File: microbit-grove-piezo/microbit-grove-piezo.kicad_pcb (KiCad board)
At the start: 2 copper layers, 59 x 15.4 mm, 6 parts, among them J1 microbit_smd_socket, J2 0 13 + 1, J3 1 14 + -, J4 2 15 + -, J5 19 20 I2C + -

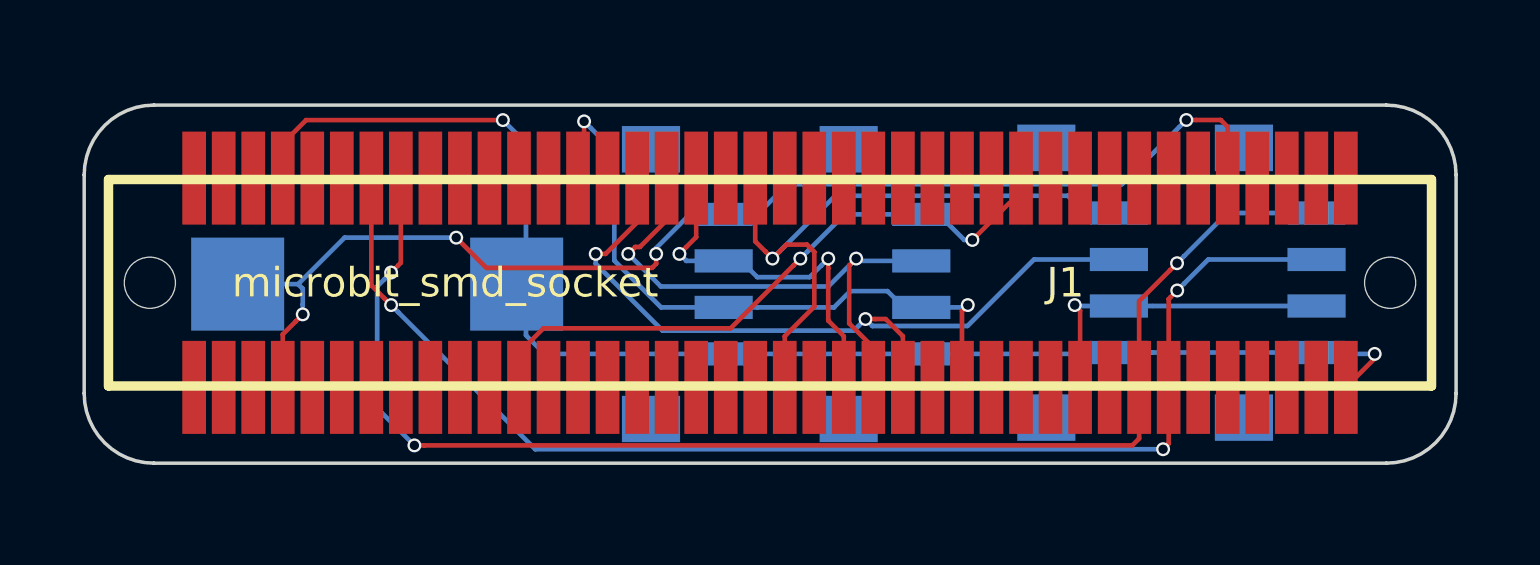
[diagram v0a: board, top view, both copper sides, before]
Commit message: Add logos to grove/piezo board
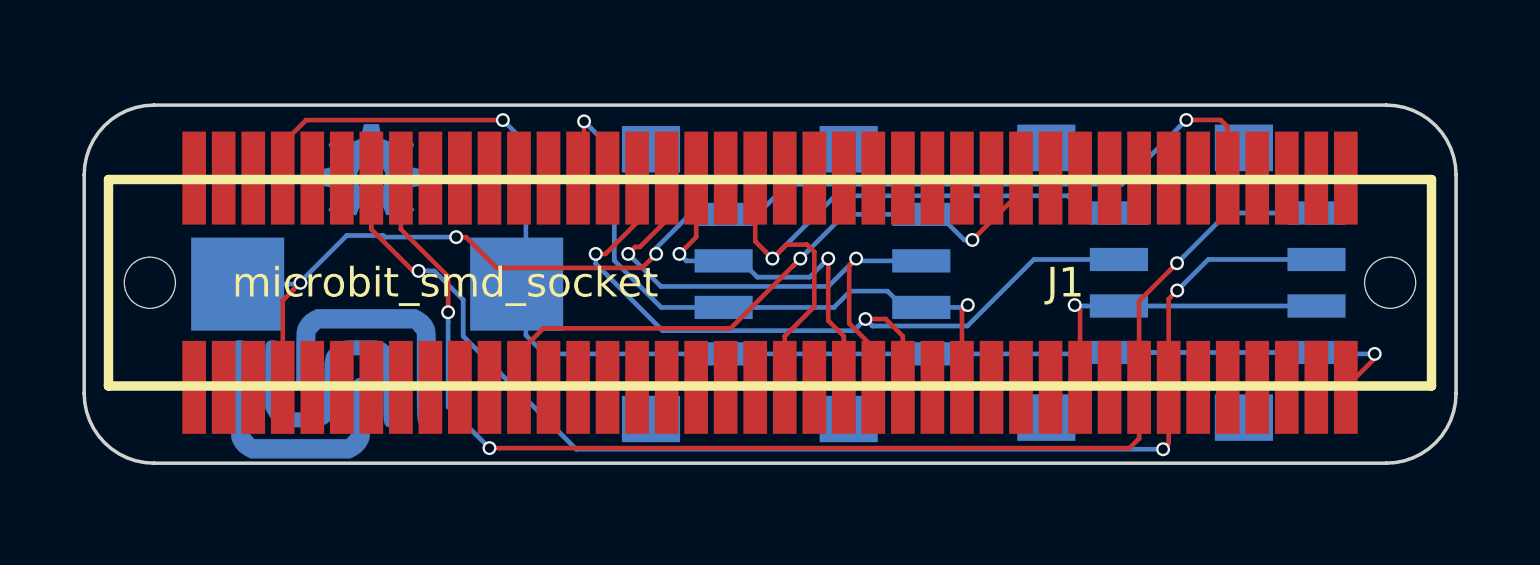
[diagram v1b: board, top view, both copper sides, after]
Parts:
- added Z1: ncss, logos:ncss, B.Cu at (131.6, 95.5)
- added Z2: oshw, logos:OSHW-Logo2_7.3x6mm_Copper, B.Cu at (133.3, 87.4)
- J2: value 0 13 + 1 -> GROVE-CONNECTOR-SMD_4+2P-2.0_
- J3: value 1 14 + - -> GROVE-CONNECTOR-SMD_4+2P-2.0_
- J4: value 2 15 + - -> GROVE-CONNECTOR-SMD_4+2P-2.0_
- J5: value 19 20 I2C + - -> GROVE-CONNECTOR-SMD_4+2P-2.0_
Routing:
- net MB_19: track 59.0 -> 56.4 mm

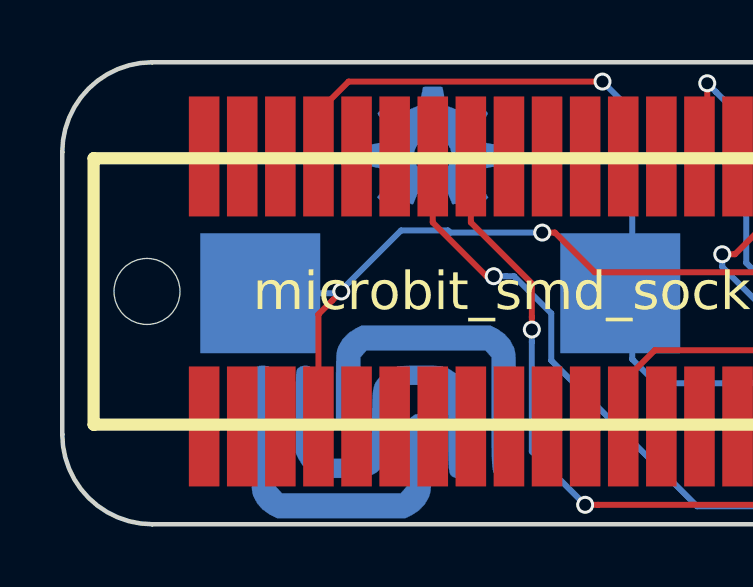
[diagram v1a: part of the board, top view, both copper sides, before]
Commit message: Make small logos for the grove board.
Test run gerbers.
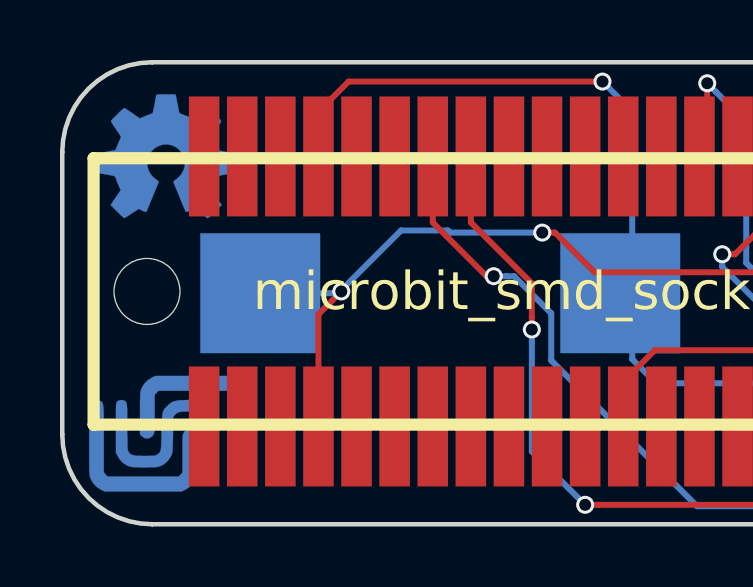
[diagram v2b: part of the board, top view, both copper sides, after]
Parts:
- Z1: footprint logos:ncss -> logos:ncss_small
- Z2: footprint logos:OSHW-Logo2_7.3x6mm_Copper -> logos:OSHW-Logo2_7.3x6mm_Copper_NoText
- moved Z2 8.89 mm to (124.5, 87.6)
- moved Z1 7.13 mm to (124.5, 96.0)
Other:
- board text added: "0 13 + -"
- board text added: "1 14 + -"
- board text added: "19 20 I2C + -"
- board text added: "2 15 + -"
- board text added: "github.com/jimmo/microbit-boards"

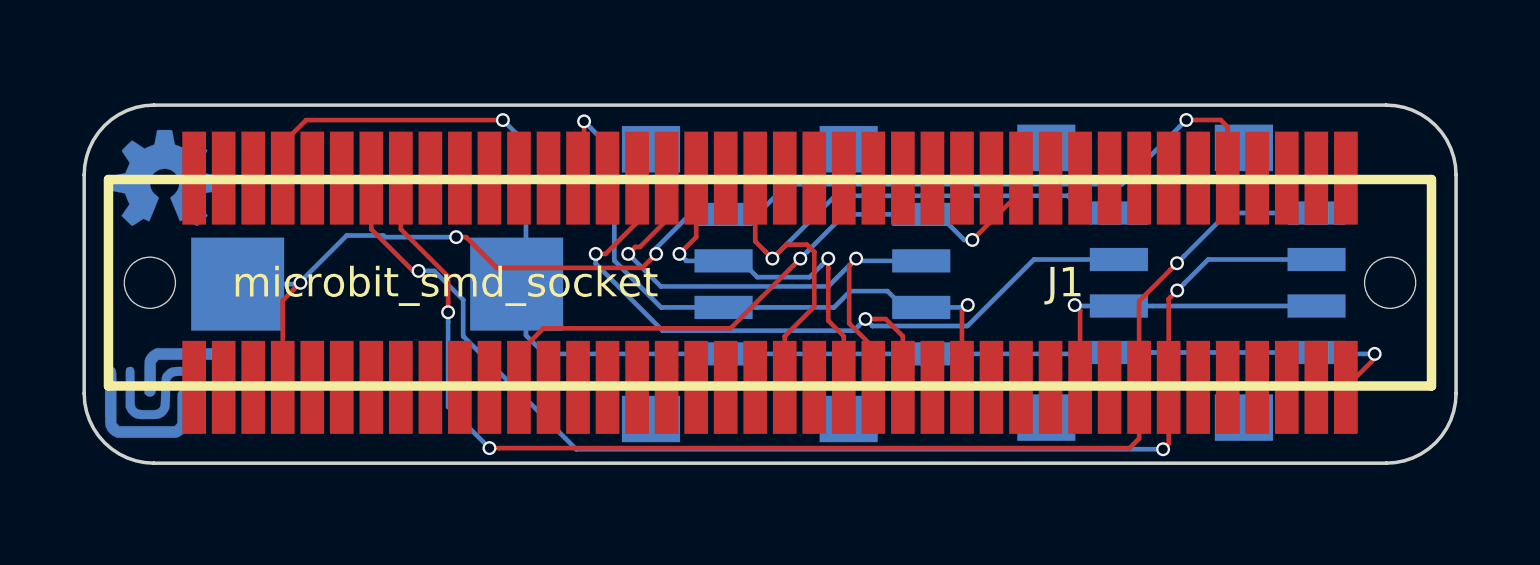
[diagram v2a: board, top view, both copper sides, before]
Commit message: Replace vcc/gnd with pours.
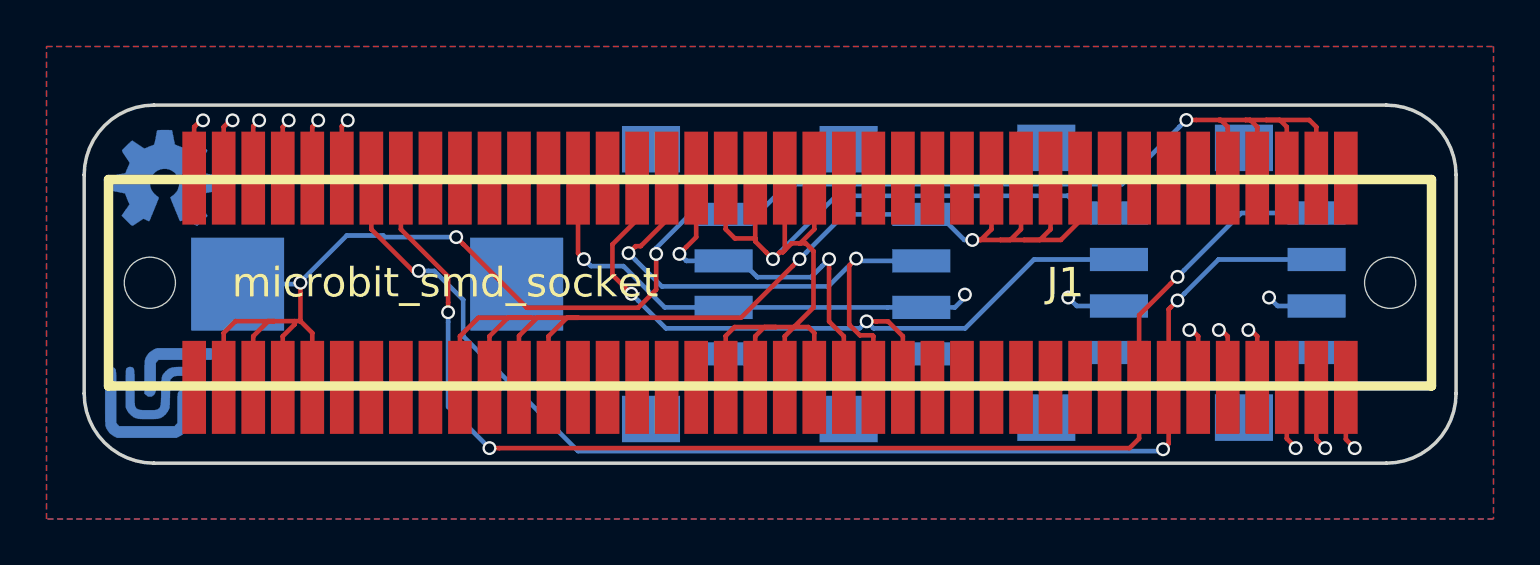
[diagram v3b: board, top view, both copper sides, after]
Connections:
- J1 pad 10: MB_9 -> (no net)
- J1 pad 11: MB_10 -> (no net)
- J1 pad 12: MB_11 -> (no net)
- J1 pad 13: MB_12 -> (no net)
- J1 pad 17: MB_16 -> (no net)
- J1 pad 29: MB_3 -> (no net)
- J1 pad 30: MB_4 -> (no net)
- J1 pad 31: MB_5 -> (no net)
- J1 pad 32: MB_6 -> (no net)
- J1 pad 33: MB_7 -> (no net)
- J1 pad 34: MB_8 -> (no net)
- J1 pad 35: MB_9 -> (no net)
- J1 pad 36: MB_10 -> (no net)
- J1 pad 37: MB_11 -> (no net)
- J1 pad 38: MB_12 -> (no net)
- J1 pad 4: MB_3 -> (no net)
- J1 pad 42: MB_16 -> (no net)
- J1 pad 5: MB_4 -> (no net)
- J1 pad 6: MB_5 -> (no net)
- J1 pad 7: MB_6 -> (no net)
- J1 pad 8: MB_7 -> (no net)
- J1 pad 9: MB_8 -> (no net)
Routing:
- net MB_GND: track 72.6 -> 32.1 mm, vias 2 -> 12
- net MB_3V3: track 56.1 -> 25.7 mm, vias 3 -> 4
- net MB_1: track 33.8 -> 56.0 mm
- net MB_0: track 61.3 -> 80.7 mm
- net MB_2: track 36.2 -> 50.5 mm
- net MB_15: track 34.0 -> 32.8 mm
- added copper zone on F.Cu, net MB_3V3
- added copper zone on B.Cu, net MB_GND
